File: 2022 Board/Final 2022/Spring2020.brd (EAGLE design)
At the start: 63 x 65 mm, 21 parts, among them U1 TB67H401FTG(O,EL), U2 ABX00012

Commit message: Almost completely working board
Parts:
- removed CVM1: 860010674014, Test:CAP_4014_WRE
- added 5V1, 5V2: (no value), pinhead:1X02
- added C1: CL05A105KP5NNNC, SnapEDA Library:CAPC1005X55N
- C2: value (none) -> CL05A105KP5NNNC; device resistor:C025-050X050 -> SnapEDA Library:CAPC1005X55N
- C3: value (none) -> UVY1H102MHD; device resistor:C025-050X050 -> Test2:CAP_12.5_X_25_NCH
- moved CVM2 63.0 mm to (16.2, 30.5), turned to 90 degrees
- moved FRT_MTR 49.3 mm to (10.5, 49.6), turned to 270 degrees
- moved U1 48.4 mm to (22.0, 40.5), turned to 270 degrees
- moved COSC 46.3 mm to (27.0, 40.0), turned to 270 degrees
- moved RRS 45.3 mm to (21.4, 31.5), turned to 90 degrees
- moved ROSC 43.7 mm to (27.0, 42.0), turned to 270 degrees
- moved REAR_PWR 43.4 mm to (10.6, 25.9), turned to 270 degrees
- moved C3 33.9 mm to (10.7, 38.0), turned to 270 degrees
- moved IMU 28.3 mm to (62.5, 49.3)
- moved U$2 21.1 mm to (36.5, 43.0), turned to 90 degrees
- moved FRT_ENCODE 19.4 mm to (50.4, 49.7), turned to 180 degrees
- moved REAR-MOTOR 19.4 mm to (34.4, 49.8)
- moved U$7 16.9 mm to (31.2, 42.9), turned to 90 degrees
- moved C2 15.6 mm to (33.7, 47.2), turned to 0 degrees
- moved PWR_IN 10.8 mm to (10.5, 15.2), turned to 270 degrees
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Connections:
- removed net N$10: FRT_ENCODE.8
- removed net N$4: FRT_ENCODE.4
- removed net N$6: U2.20
- removed net N$7: U2.21
- new net FLMT: FRT_ENCODE.4, U2.7
- new net RLMT: FRT_ENCODE.8, U2.8
- net 3.3V: now also C1.1; no longer C2.1
- net 5V: now also 5V1.2, 5V2.2, C2.2; no longer C3.1
- net BKPWR: now also C3.2, PWR_IN.1, REAR_PWR.2; no longer CVM1.2, PWR_IN.2, REAR_PWR.1
- net F+: now also FRT_MTR.1; no longer FRT_MTR.2
- net F-: now also FRT_MTR.2; no longer FRT_MTR.1
- net FRT_PWM: now also U2.14
- net GND: now also 5V1.1, 5V2.1, C1.2, C2.1, C3.1, PWR_IN.2, REAR-MOTOR.4, REAR_PWR.1; no longer C2.2, C3.2, CVM1.1, PWR_IN.1, REAR-MOTOR.1, REAR_PWR.2
- net IMU-CS: now also IMU.4, U2.20; no longer IMU.2, U2.16
- net I_1: now also U2.13
- net I_2: now also U2.12
- net QUAD-A: now also U2.16
- net QUAD-B: now also U2.15
- net REAR-PWM: now also U2.9; no longer U2.12
- net REAR-PWMOUT: now also REAR-MOTOR.1; no longer REAR-MOTOR.2
- net REAR-TIMER: now also REAR-MOTOR.3; no longer REAR-MOTOR.4
- net REAR-TIMER-IN: now also U2.21
- net REVERSE: now also REAR-MOTOR.2; no longer REAR-MOTOR.3
- net SCK: now also IMU.2; no longer IMU.4
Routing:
- net GND: track 0.00 -> 184.3 mm
- net BKPWR: track 0.00 -> 75.2 mm
- net 5V: track 0.00 -> 60.2 mm
- net RS: track 0.00 -> 49.9 mm
- net F+: track 0.00 -> 41.3 mm
- net F-: track 0.00 -> 22.0 mm, vias 0 -> 1
- net 3.3V: track 0.00 -> 8.69 mm
- net REVERSE: track 0.00 -> 5.00 mm
- net REAR-TIMER: track 0.00 -> 4.48 mm
- net REAR-PWMOUT: track 0.00 -> 3.68 mm
- net REAR-PWM-5V: track 0.00 -> 1.39 mm
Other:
- board size 63 x 65 mm -> 76 x 45 mm

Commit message: Just a few random edits
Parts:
- moved IMU 2.00 mm to (60.5, 49.3)
- moved RC 2.00 mm to (71.5, 49.2)
- moved PS1 1.50 mm to (74.5, 15.0)
- moved ROSC 1.44 mm to (27.3, 40.6), turned to 180 degrees
- moved COSC 0.64 mm to (27.5, 39.6), turned to 0 degrees
- renumbered C3 to CMV1
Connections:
- net FLMT: no longer U2.7
- net FRT_PWM: now also U2.9; no longer U2.14
- net I_1: now also U2.11; no longer U2.13
- net I_2: now also U2.10; no longer U2.12
- net QUAD-A: now also U2.15; no longer U2.16
- net QUAD-B: now also U2.16; no longer U2.15
- net REAR-PWM: now also U2.12; no longer U2.9
- net REAR-TIMER-IN: now also U2.13; no longer U2.10, U2.21
- net REVERSE_IN: now also U2.14; no longer U2.11
- net RLMT: no longer U2.8
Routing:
- net GND: track 184.3 -> 297.9 mm
- net 5V: track 60.2 -> 173.7 mm, vias 0 -> 3
- net 3.3V: track 8.69 -> 112.6 mm, vias 0 -> 1
- net I_2: track 0.00 -> 39.5 mm, vias 0 -> 1
- net I_1: track 0.00 -> 37.9 mm, vias 0 -> 1
- net QUAD-A: track 0.00 -> 35.3 mm
- net QUAD-B: track 0.00 -> 32.9 mm
- net SCK: track 0.00 -> 30.5 mm
- net IMU-CS: track 0.00 -> 30.1 mm
- net MOSI: track 0.00 -> 27.7 mm
- net MISO: track 0.00 -> 26.6 mm
- net REAR-PWM: track 0.00 -> 24.3 mm
- net FRT_PWM: track 0.00 -> 16.8 mm
- net REAR-TIMER-IN: track 0.00 -> 15.8 mm
- net REVERSE_IN: track 0.00 -> 13.9 mm
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
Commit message: DONE!
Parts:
- removed U$2, U$7: IL-712, Spring2016Optoisolator:8PINSOIC
- added ISO_1, ISO_2: π121U31, SnapEDA Library:SO08
- FRT_ENCODE: device Test:CONN_3220-10-0100-00_CNC -> SnapEDA Library:CONN_3220-10-0100-00_CNC
- FRT_MTR, PWR_IN, REAR_PWR: value 1792863 -> 2060-452_998-404; device Test:CONN_1792863_PXC -> 2060-452_998-404:2060452998404
- ROSC: value RC0100JR-075K1L -> (none); device SnapEDA Library:RESC0402X15N -> rcl:R0402
- moved REAR_PWR 5.57 mm to (11.1, 20.3), turned to 0 degrees
- moved FRT_MTR 4.34 mm to (8.53, 45.7), turned to 0 degrees
- moved C1 3.99 mm to (34.4, 34.9)
- moved PWR_IN 3.27 mm to (11.0, 12.0), turned to 0 degrees
- moved REAR-MOTOR 3.17 mm to (34.2, 46.6)
- moved C2 2.68 mm to (33.6, 44.6)
- moved RRS 2.67 mm to (21.3, 28.8)
- moved U1 2.67 mm to (21.9, 37.8)
- moved CVM2 2.67 mm to (16.1, 27.8)
- moved COSC 2.67 mm to (27.4, 37.0)
- moved CMV1 2.62 mm to (11.7, 35.6)
- moved PWM 2.55 mm to (30.4, 44.5)
- moved R-PWM-C 2.55 mm to (31.9, 44.5)
- moved ROSC 2.42 mm to (27.1, 38.1)
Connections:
- net 3.3V: now also ISO_1.1, ISO_2.1; no longer U$2.1, U$7.1
- net 5V: now also ISO_1.8, ISO_2.8; no longer U$2.8, U$7.8
- net BKPWR: now also PWR_IN.3, REAR_PWR.4
- net F+: now also FRT_MTR.2, FRT_MTR.4; no longer FRT_MTR.1
- net F-: now also FRT_MTR.1, FRT_MTR.3; no longer FRT_MTR.2
- net GND: now also ISO_1.4, ISO_1.5, ISO_2.4, ISO_2.5, PWR_IN.4, REAR_PWR.3; no longer U$2.4, U$2.5, U$7.4, U$7.5
- net REAR-PWM: now also ISO_2.2; no longer U$7.2
- net REAR-PWM-5V: now also ISO_2.7; no longer U$7.7
- net REAR-TIMER: now also ISO_1.6; no longer U$2.6
- net REAR-TIMER-IN: now also ISO_1.3; no longer U$2.3
- net REVERSE: now also ISO_1.7; no longer U$2.7
- net REVERSE_IN: now also ISO_1.2; no longer U$2.2
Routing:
- net GND: track 297.9 -> 375.7 mm, vias 0 -> 4
- net BKPWR: track 78.4 -> 106.1 mm
- net 5V: track 173.7 -> 189.7 mm, vias 3 -> 0
- net 3.3V: track 112.6 -> 98.5 mm
- net F+: track 41.3 -> 55.3 mm
- net RS: track 50.8 -> 62.1 mm
- net QUAD-B: track 32.9 -> 41.7 mm
- net REAR-PWM: track 24.3 -> 28.9 mm
- net F-: track 22.0 -> 25.7 mm, vias 1 -> 0
- net REAR-TIMER-IN: track 15.8 -> 18.7 mm
- net QUAD-A: track 35.3 -> 38.1 mm
- net REVERSE_IN: track 13.9 -> 15.8 mm
- net MISO: track 26.6 -> 28.0 mm
- net MOSI: track 27.7 -> 28.9 mm
- net I_1: track 37.9 -> 39.0 mm
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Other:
- board size 76 x 45 mm -> 75.9 x 45 mm

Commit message: Almost done
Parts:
- added RRS1: RLP73K3AR22FTDF, SnapEDA Library:RESC6331X70N
- RRS: value CSRL3-0R15F8 -> RLP73K3AR22FTDF; device Test:RES_CSRL3_3-200MOHM_RDN -> SnapEDA Library:RESC6331X70N
- moved CVM2 1.88 mm to (15.8, 25.9)
- moved RRS 0.50 mm to (21.3, 29.3)
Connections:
- net BKPWR: now also RRS1.1
- net RS: now also RRS1.2
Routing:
- net BKPWR: track 106.1 -> 118.7 mm
- net 3.3V: track 98.5 -> 88.5 mm
- net RS: track 62.1 -> 64.4 mm
- net GND: track 375.7 -> 377.6 mm
- net 5V: track 189.7 -> 189.0 mm

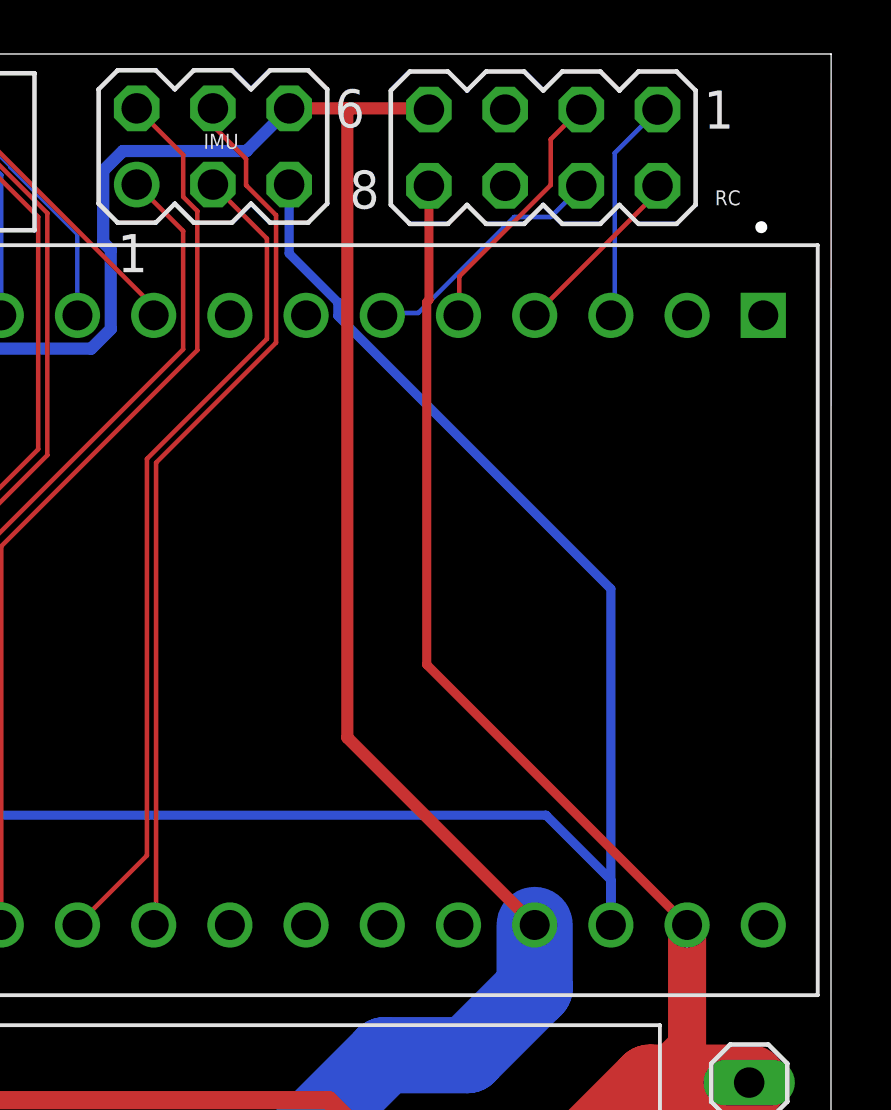
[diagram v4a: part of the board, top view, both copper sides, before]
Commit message: Changed IMU voltage
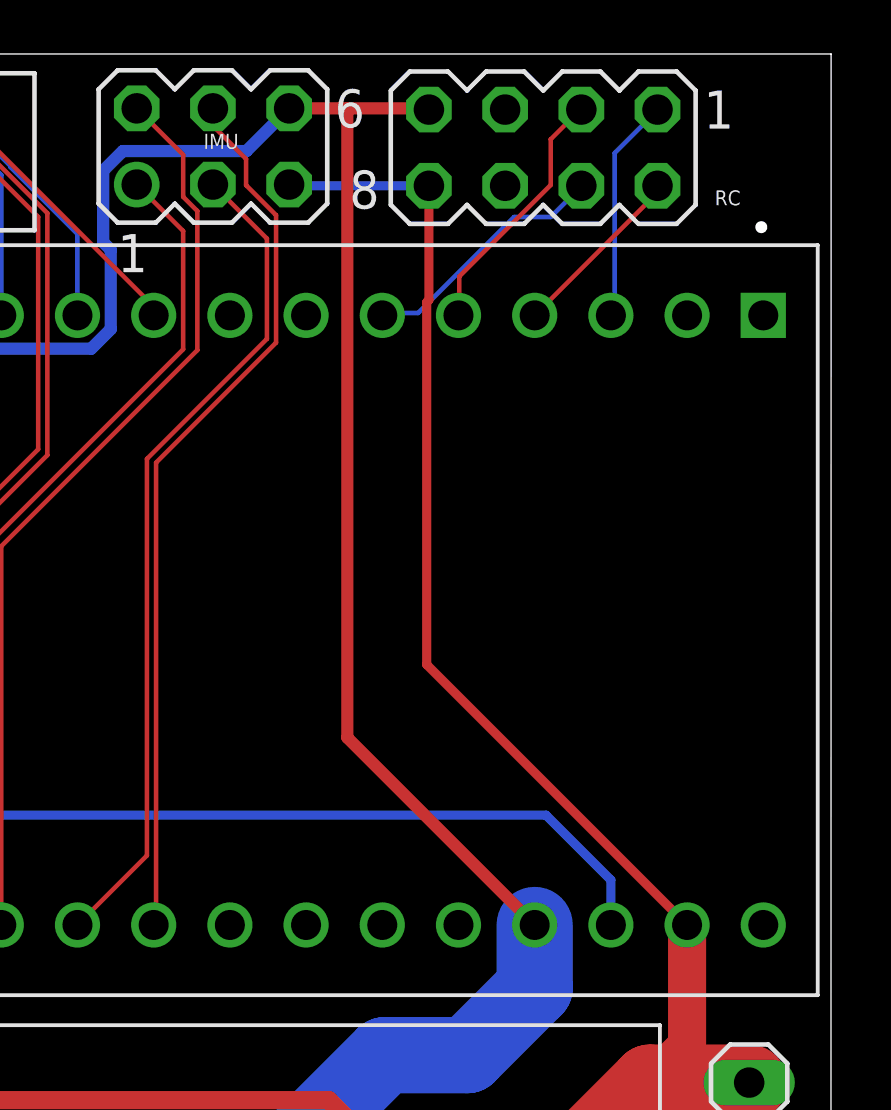
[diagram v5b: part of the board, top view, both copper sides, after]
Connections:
- net 3.3V: no longer IMU.5
- net 5V: now also IMU.5
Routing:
- net 3.3V: track 88.5 -> 59.4 mm
- net 5V: track 189.0 -> 193.7 mm
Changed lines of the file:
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@@
 <signal name="3.3V">
 <contactref element="U2" pad="26"/>
-<contactref element="IMU" pad="5"/>
 <contactref element="C1" pad="1"/>
 <contactref element="U1" pad="42"/>
-<wire x1="73.7852" y1="23.34" x2="73.7852" y2="34.542625" width="0.3048" layer="16"/>
-<wire x1="64.684" y1="43.643825" x2="64.684" y2="44.098575" width="0.3048" layer="16"/>
-<wire x1="63.06" y1="45.722575" x2="63.06" y2="48.02" width="0.3048" layer="16"/>
-<wire x1="64.684" y1="44.098575" x2="63.06" y2="45.722575" width="0.3048" layer="16"/>
-<wire x1="73.7852" y1="34.542625" x2="64.684" y2="43.643825" width="0.3048" layer="16"/>
 <wire x1="43.206" y1="27" x2="71.6252" y2="27" width="0.3048" layer="16"/>
 <wire x1="43.206" y1="27" x2="36.248" y2="33.958" width="0.3048" layer="16"/>
@@
 <wire x1="37.625" y1="23.5" x2="37.607753125" y2="23.482753125" width="0.1524" layer="1"/>
 <wire x1="37.625" y1="23.5" x2="37.7682" y2="23.30701875" width="0.1524" layer="1"/>
+<contactref element="IMU" pad="5"/>
+<wire x1="67.72" y1="47.979" x2="63.101" y2="47.979" width="0.3048" layer="16"/>
+<wire x1="63.101" y1="47.979" x2="63.06" y2="48.02" width="0.1524" layer="16"/>
 </signal>
 <signal name="BKPWR">
